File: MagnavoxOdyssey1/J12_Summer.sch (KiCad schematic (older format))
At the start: 15 parts

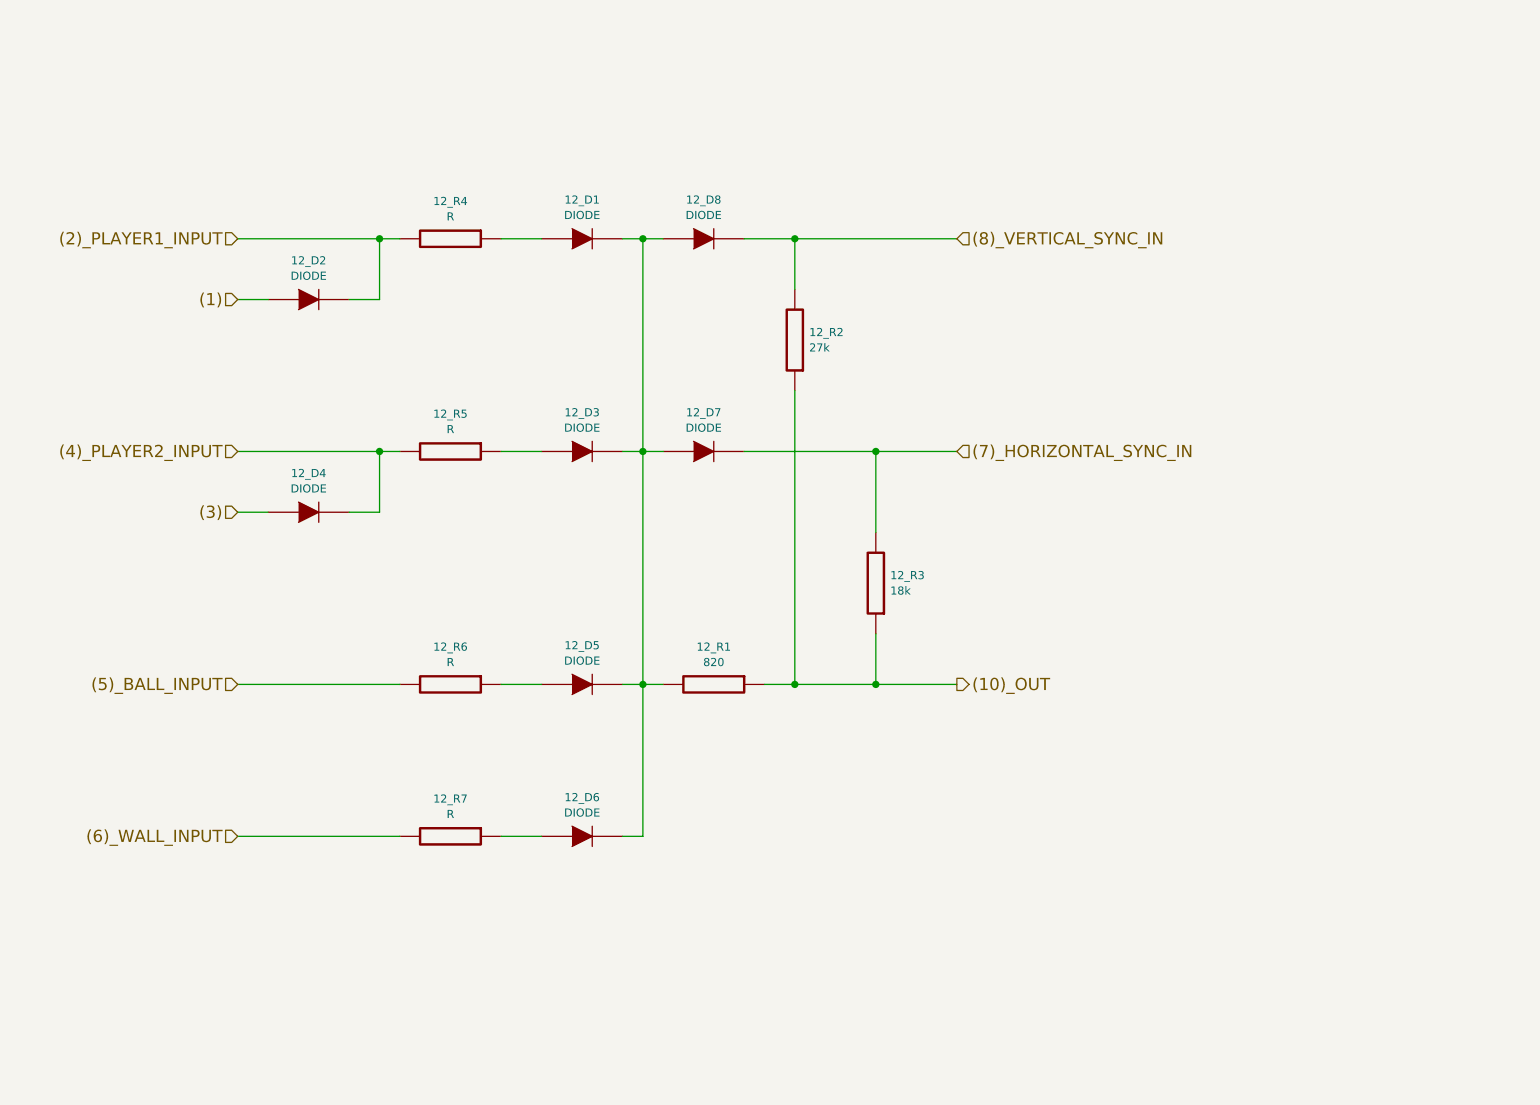
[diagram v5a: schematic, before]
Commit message: terminei de transcrever a PCB toda. Deixei de fora de propósito o estágio de modulação RF do sinal. É pouca coisa, posso adicionar amanhã ou depois... Gerei também um PDFão
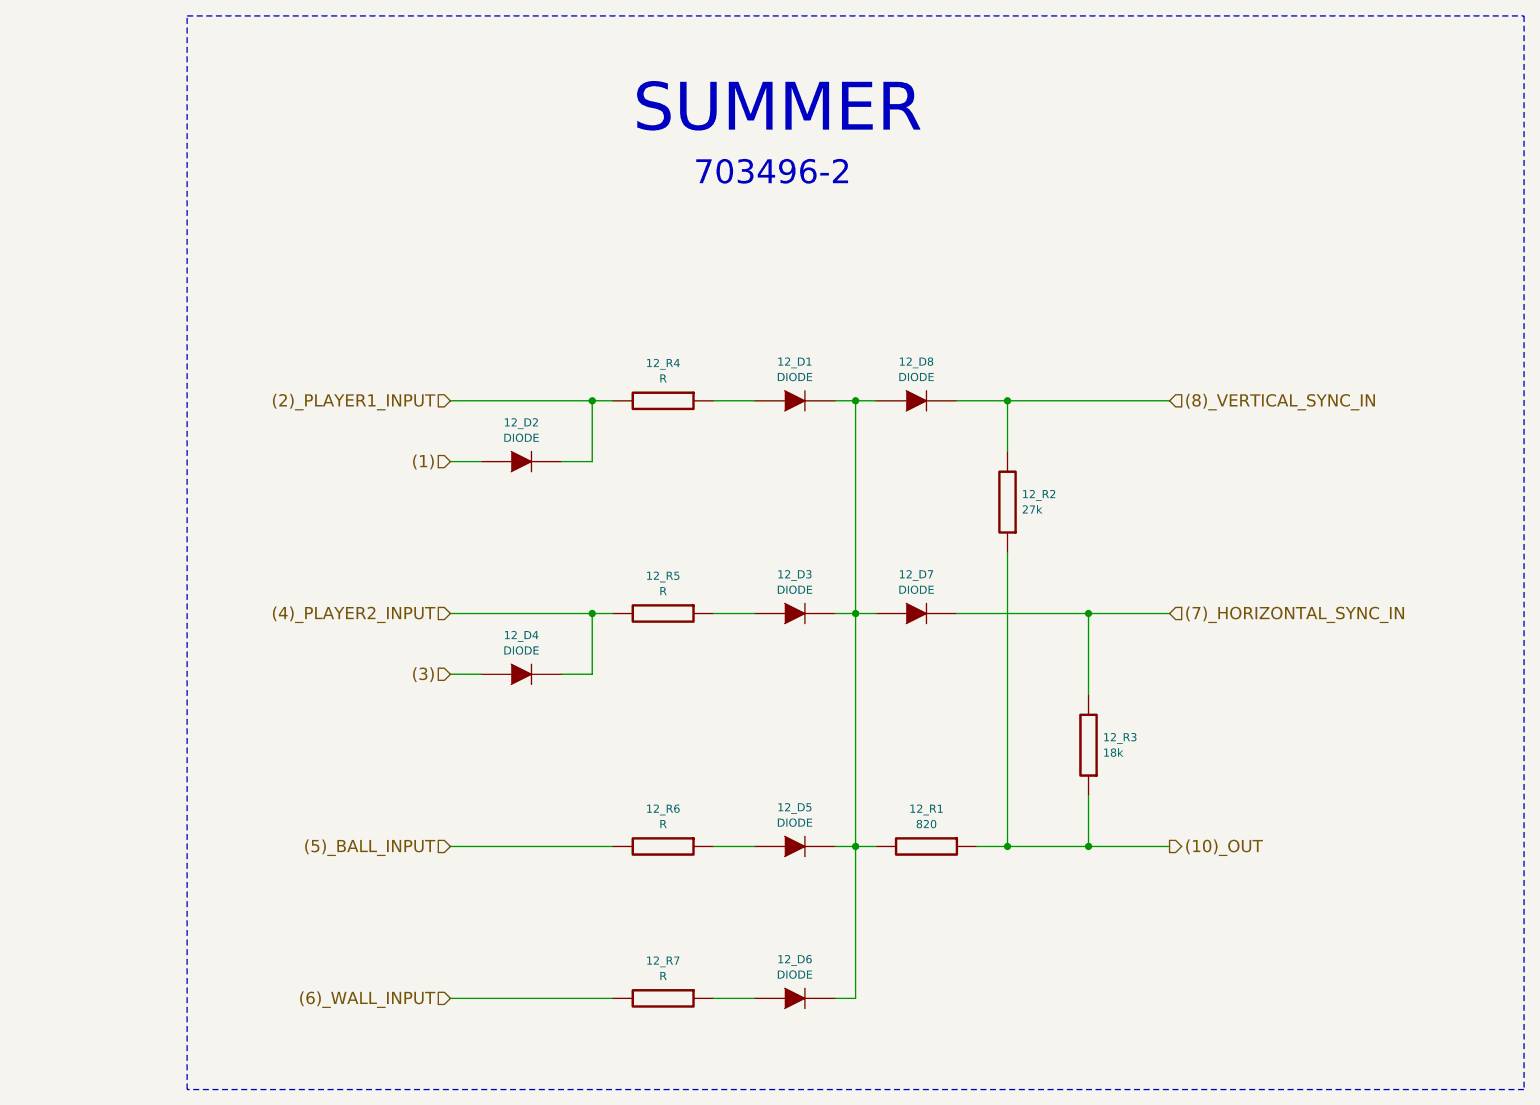
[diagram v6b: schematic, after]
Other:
- note added: "703496-2"
- note added: "SUMMER"
- moved on the sheet: 12_D1, 12_D2, 12_D3, 12_D4, 12_D5, 12_D6, 12_D7, 12_D8, 12_R1, 12_R2, 12_R3, 12_R4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
